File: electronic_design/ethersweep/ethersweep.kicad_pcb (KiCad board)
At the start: 2 copper layers, 79 x 38 mm, 102 parts, among them J1 AVR-ISP-6, J10 HR911105A, J11 B4B-XH-A(LF)(SN), J2 Conn_01x02_Male, J3 Conn_01x04_Female, J4 Conn_01x02_Male, J5 Conn_01x02_Male, J6 Conn_01x07_Female, J7 Conn_01x07_Male, J8 AVR-ISP-6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

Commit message: added 3d cad files, production files, for 3.0.4
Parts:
- removed M1: Stepper_Motor_bipolar, Connector_PinHeader_2.54mm:PinHeader_2x02_P2.54mm_Vertical_SMD
- J11: value B4B-XH-A(LF)(SN) -> Conn_01x04_Male; footprint modules:JST_B4B-XH-A(LF)(SN) -> Connector_JST:JST_EH_S4B-EH_1x04_P2.50mm_Horizontal
- moved J11 33.1 mm to (209.7, 18.1)
- moved C19 2.75 mm to (202.2, 55.1), turned to 0 degrees
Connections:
- U3 pad 1: Net-(M1-Pad4) -> Net-(J11-Pad1)
- U3 pad 21: Net-(M1-Pad2) -> Net-(J11-Pad2)
- U3 pad 24: Net-(M1-Pad1) -> Net-(J11-Pad3)
- U3 pad 26: Net-(M1-Pad3) -> Net-(J11-Pad4)
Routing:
- net Net-(M1-Pad4): track 9.00 -> 0.00 mm, vias 1 -> 0
- net Net-(M1-Pad2): track 8.87 -> 0.00 mm, vias 1 -> 0
- net voltage_detect: track 27.5 -> 23.8 mm
- net Net-(M1-Pad1): track 2.70 -> 0.00 mm, vias 1 -> 0
- net Net-(M1-Pad3): track 2.69 -> 0.00 mm, vias 1 -> 0
- net Net-(J11-Pad2): track 0.00 -> 1.10 mm, vias 0 -> 1
- net Net-(J11-Pad1): track 0.00 -> 0.84 mm, vias 0 -> 1
- net GND: vias 212 -> 210

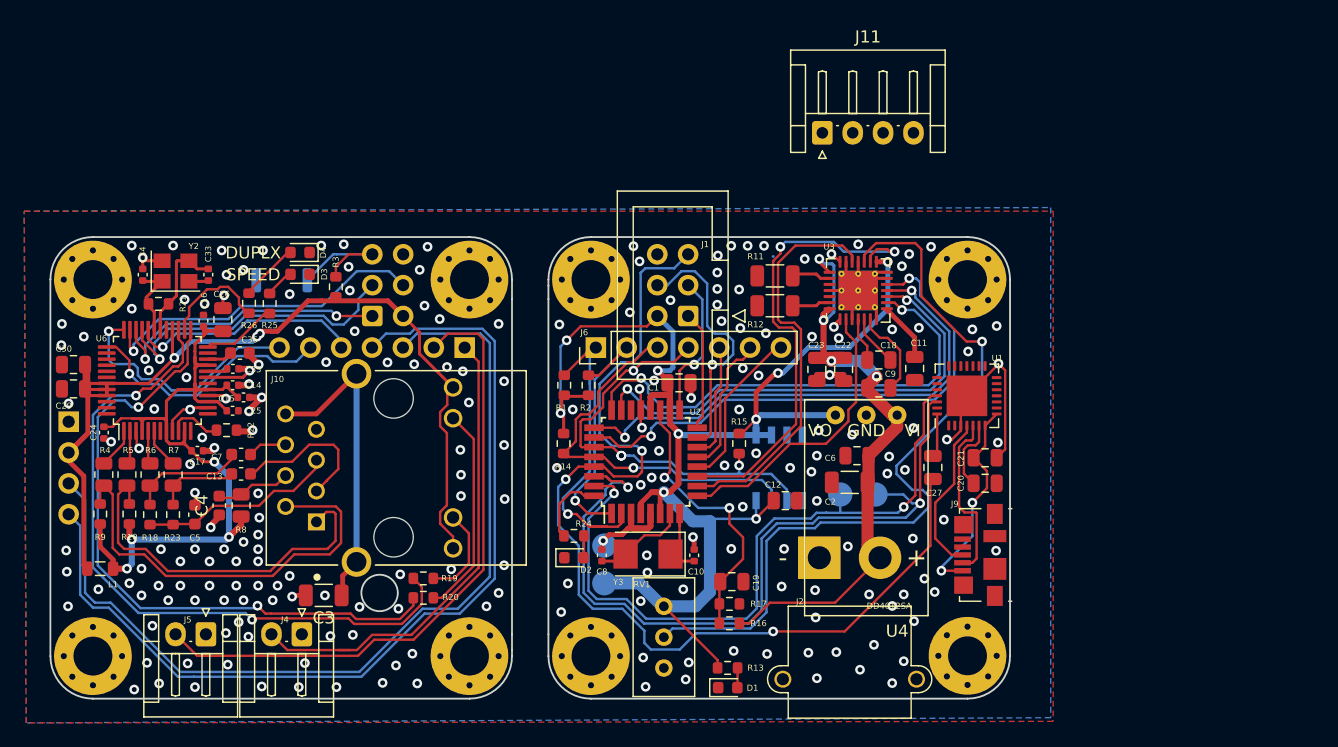
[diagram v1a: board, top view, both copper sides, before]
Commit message: removed old code + design files
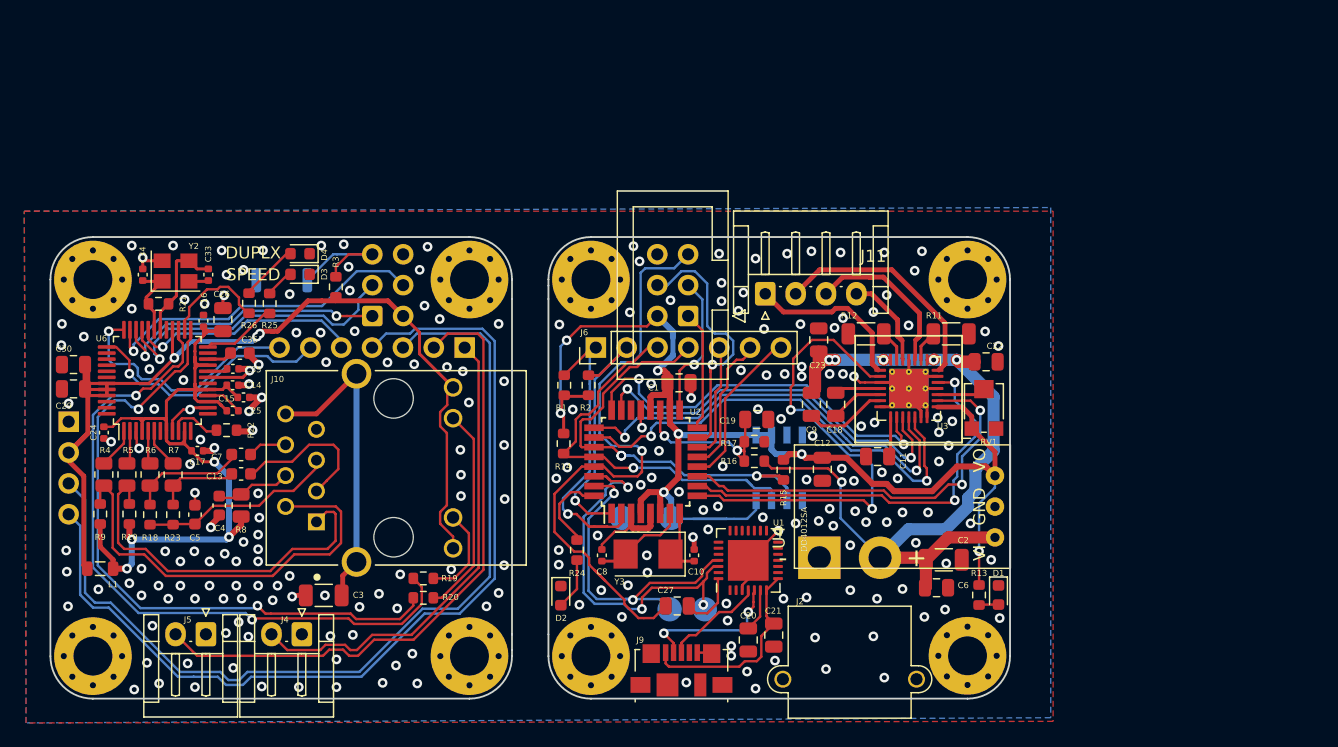
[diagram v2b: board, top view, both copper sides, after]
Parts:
- RV1: footprint Potentiometer_THT:Potentiometer_Bourns_3296W_Vertical -> Potentiometer_SMD:Potentiometer_Bourns_TC33X_Vertical
- moved RV1 31.1 mm to (222.9, 40.7)
- moved J9 26.4 mm to (198.1, 62.4), turned to 0 degrees
- moved C27 23.9 mm to (197.7, 57.1), turned to 0 degrees
- moved D1 23.6 mm to (224.2, 56.2), turned to -90 degrees
- moved C20 23.4 mm to (203.6, 59.9), turned to -90 degrees
- moved C21 22.7 mm to (205.7, 59.5), turned to -90 degrees
- moved U1 22.5 mm to (203.6, 53.3)
- moved R13 21.6 mm to (222.6, 56.2), turned to -90 degrees
- moved G*** 18.5 mm to (215.2, 41.8), turned to -90 degrees
- moved TP3 16.9 mm to (200.0, 57.3)
- moved TP4 16.9 mm to (197.1, 57.3)
- moved R11 15.3 mm to (220.2, 34.7), turned to 0 degrees
- moved J11 14.1 mm to (204.9, 31.4)
- moved C19 13.5 mm to (204.2, 41.7)
- moved R16 13.5 mm to (204.1, 45.1)
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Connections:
- J9 pad 4: Net-(J9-Pad4) -> unconnected-(J9-Pad4)
- U1 pad 1: Net-(U1-Pad1) -> unconnected-(U1-Pad1)
- U1 pad 10: Net-(U1-Pad10) -> unconnected-(U1-Pad10)
- U1 pad 11: Net-(U1-Pad11) -> unconnected-(U1-Pad11)
- U1 pad 12: Net-(U1-Pad12) -> unconnected-(U1-Pad12)
- U1 pad 13: Net-(U1-Pad13) -> unconnected-(U1-Pad13)
- U1 pad 14: Net-(U1-Pad14) -> unconnected-(U1-Pad14)
- U1 pad 15: Net-(U1-Pad15) -> unconnected-(U1-Pad15)
- U1 pad 16: Net-(U1-Pad16) -> unconnected-(U1-Pad16)
- U1 pad 17: Net-(U1-Pad17) -> unconnected-(U1-Pad17)
- U1 pad 18: Net-(U1-Pad18) -> unconnected-(U1-Pad18)
- U1 pad 19: Net-(U1-Pad19) -> unconnected-(U1-Pad19)
- U1 pad 2: Net-(U1-Pad2) -> unconnected-(U1-Pad2)
- U1 pad 20: Net-(U1-Pad20) -> unconnected-(U1-Pad20)
- U1 pad 21: Net-(U1-Pad21) -> unconnected-(U1-Pad21)
- U1 pad 22: Net-(U1-Pad22) -> unconnected-(U1-Pad22)
- U1 pad 23: Net-(U1-Pad23) -> unconnected-(U1-Pad23)
- U1 pad 24: Net-(U1-Pad24) -> unconnected-(U1-Pad24)
- U1 pad 27: Net-(U1-Pad27) -> unconnected-(U1-Pad27)
- U1 pad 9: Net-(U1-Pad9) -> unconnected-(U1-Pad9)
- U2 pad 22: Net-(U2-Pad22) -> unconnected-(U2-Pad22)
- U5 pad 3: Net-(U5-Pad3) -> unconnected-(U5-Pad3)
- U5 pad 5: Net-(U5-Pad5) -> unconnected-(U5-Pad5)
- U6 pad 12: Net-(U6-Pad12) -> unconnected-(U6-Pad12)
- U6 pad 13: Net-(U6-Pad13) -> unconnected-(U6-Pad13)
- U6 pad 18: Net-(U6-Pad18) -> unconnected-(U6-Pad18)
- U6 pad 23: Net-(U6-Pad23) -> unconnected-(U6-Pad23)
- U6 pad 38: Net-(U6-Pad38) -> unconnected-(U6-Pad38)
- U6 pad 39: Net-(U6-Pad39) -> unconnected-(U6-Pad39)
- U6 pad 40: Net-(U6-Pad40) -> unconnected-(U6-Pad40)
- U6 pad 41: Net-(U6-Pad41) -> unconnected-(U6-Pad41)
- U6 pad 42: Net-(U6-Pad42) -> unconnected-(U6-Pad42)
- U6 pad 46: Net-(U6-Pad46) -> unconnected-(U6-Pad46)
- U6 pad 47: Net-(U6-Pad47) -> unconnected-(U6-Pad47)
- U6 pad 7: Net-(U6-Pad7) -> unconnected-(U6-Pad7)
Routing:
- net Net-(RV1-Pad2): track 64.8 -> 4.00 mm, vias 1 -> 0
- net uC_RX: track 64.8 -> 31.2 mm, vias 2 -> 3
- net rst: track 94.2 -> 62.0 mm, vias 3 -> 1
- net uC_TX: track 57.4 -> 27.7 mm
- net +12V: track 52.3 -> 70.3 mm, vias 4 -> 6
- net Net-(J11-Pad2): track 1.10 -> 19.0 mm, vias 1 -> 0
- net STEPPER_ENABLE: track 24.0 -> 40.4 mm, vias 0 -> 2
- net +3V3: track 217.2 -> 201.4 mm, vias 12 -> 10
- net Net-(J11-Pad3): track 0.00 -> 15.5 mm
- net GND: track 88.3 -> 73.4 mm, vias 210 -> 227
- net Net-(J11-Pad1): track 0.84 -> 13.6 mm, vias 1 -> 0
- net Net-(J11-Pad4): track 0.00 -> 10.3 mm
- net voltage_detect: track 23.8 -> 16.4 mm
- net M1: track 40.2 -> 32.9 mm
- net M0: track 41.7 -> 34.5 mm
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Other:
- outline, holes or cut-outs redrawn
- net class Default removed
- net class thick removed
- board text added: "2022-02-22"
- board text added: "3.3V"
- board text added: "GND"
- board text added: "rev. 3.0.4"
- board text removed: "2021-11-08"
- board text removed: "3.3V>"
- board text removed: "GND>"
- board text removed: "MOTOR"
- board text removed: "ethersweep"
- board text removed: "vers. 3.0.4"

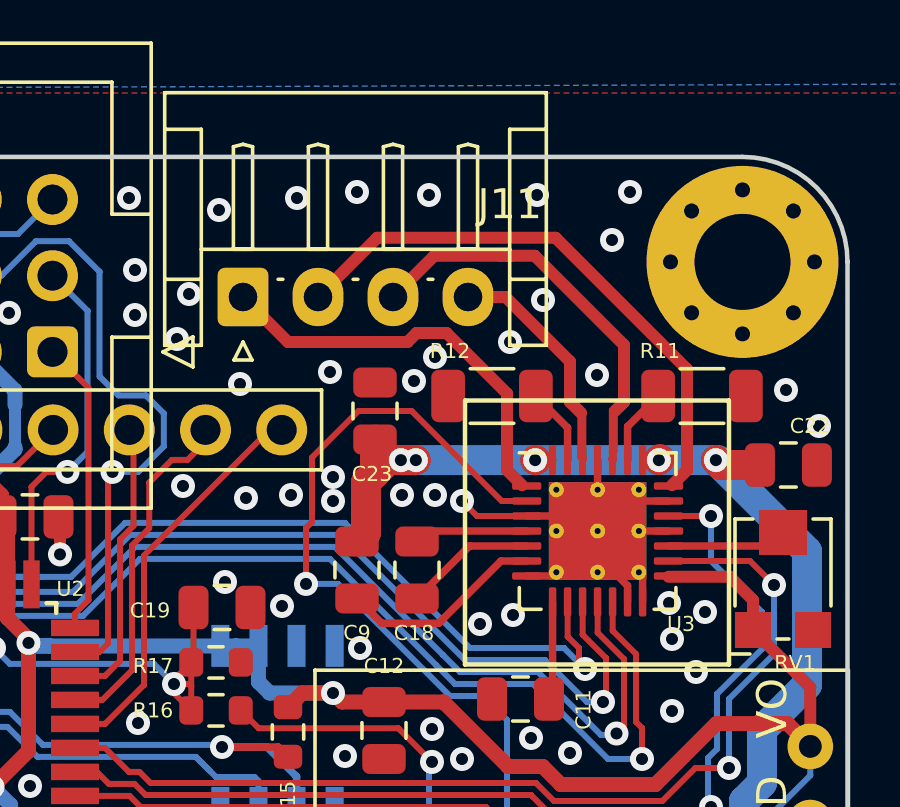
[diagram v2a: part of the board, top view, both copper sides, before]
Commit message: changed pinout for nema17 motor to be parallel to connector
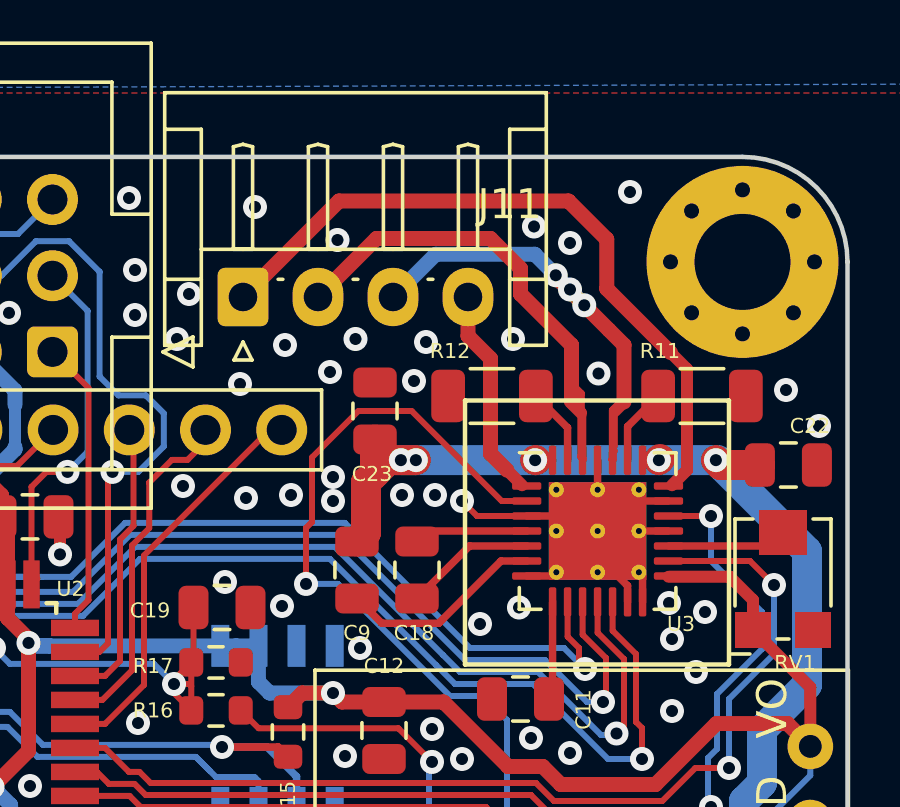
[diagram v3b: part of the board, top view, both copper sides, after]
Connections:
- U3 pad 1: Net-(J11-Pad1) -> Net-(J11-Pad4)
- U3 pad 21: Net-(J11-Pad2) -> Net-(J11-Pad1)
- U3 pad 26: Net-(J11-Pad4) -> Net-(J11-Pad2)
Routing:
- net Net-(J11-Pad1): track 13.6 -> 23.5 mm
- net Net-(J11-Pad4): track 10.3 -> 7.02 mm
- net Net-(J11-Pad3): track 15.5 -> 17.6 mm, vias 0 -> 3
- net Net-(J11-Pad2): track 19.0 -> 19.6 mm
- net GND: vias 227 -> 226
